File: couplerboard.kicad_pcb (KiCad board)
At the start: 2 copper layers, 48 x 33 mm, 15 parts, among them J1 X, J2 Y, J3 Z, J4 Conn_01x05, U1 LTV-817, U2 LTV-817, U3 LTV-817

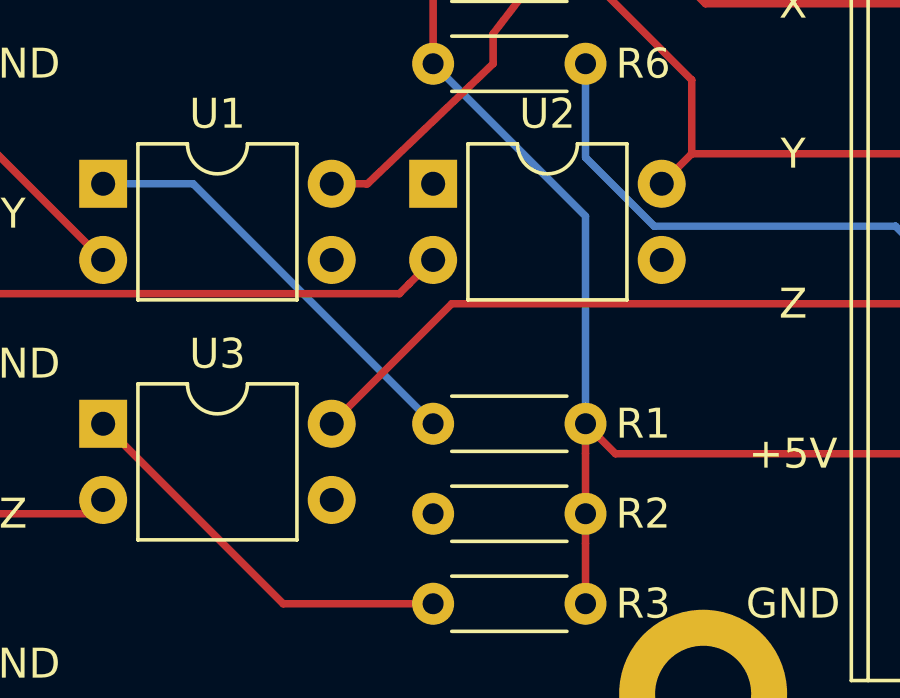
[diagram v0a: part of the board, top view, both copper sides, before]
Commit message: Fix missing route
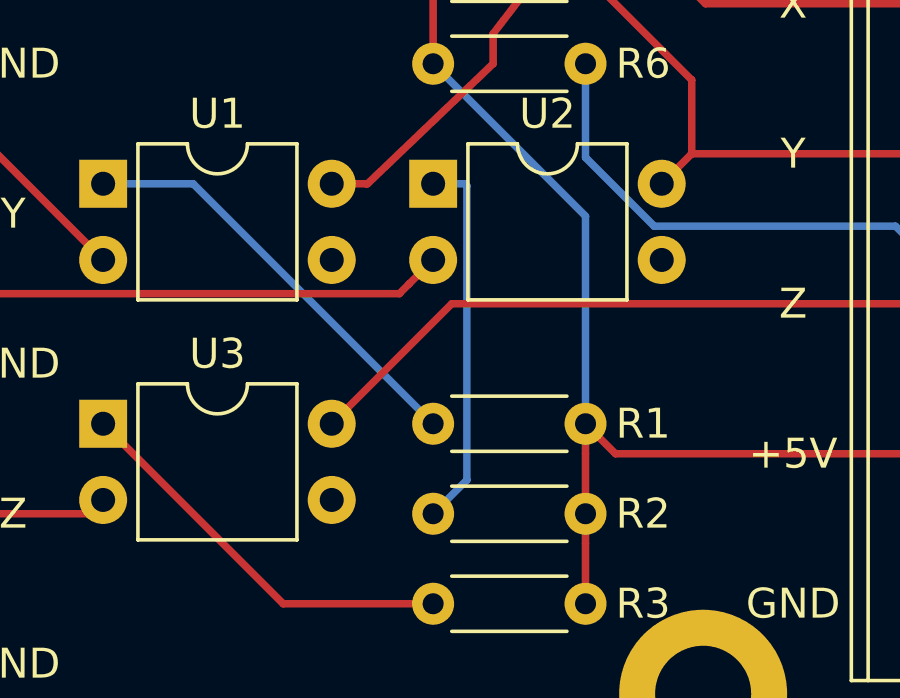
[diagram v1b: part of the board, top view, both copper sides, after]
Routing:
- net Net-(R2-Pad1): track 0.00 -> 12.5 mm
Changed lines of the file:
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@@
     (thickness 1.6)
     (drawings 15)
-    (tracks 42)
+    (tracks 46)
     (zones 0)
     (modules 15)
@@
   (segment (start 104 70) (end 112 78) (width 0.25) (layer B.Cu) (net 9))
   (segment (start 101 70) (end 104 70) (width 0.25) (layer B.Cu) (net 9))
+  (segment (start 113.05 70) (end 112 70) (width 0.25) (layer B.Cu) (net 10))
+  (segment (start 113.125001 70.075001) (end 113.05 70) (width 0.25) (layer B.Cu) (net 10))
+  (segment (start 113.125001 79.874999) (end 113.125001 70.075001) (width 0.25) (layer B.Cu) (net 10))
+  (segment (start 112 81) (end 113.125001 79.874999) (width 0.25) (layer B.Cu) (net 10))
   (segment (start 107 84) (end 101 78) (width 0.25) (layer F.Cu) (net 11))
   (segment (start 112 84) (end 107 84) (width 0.25) (layer F.Cu) (net 11))

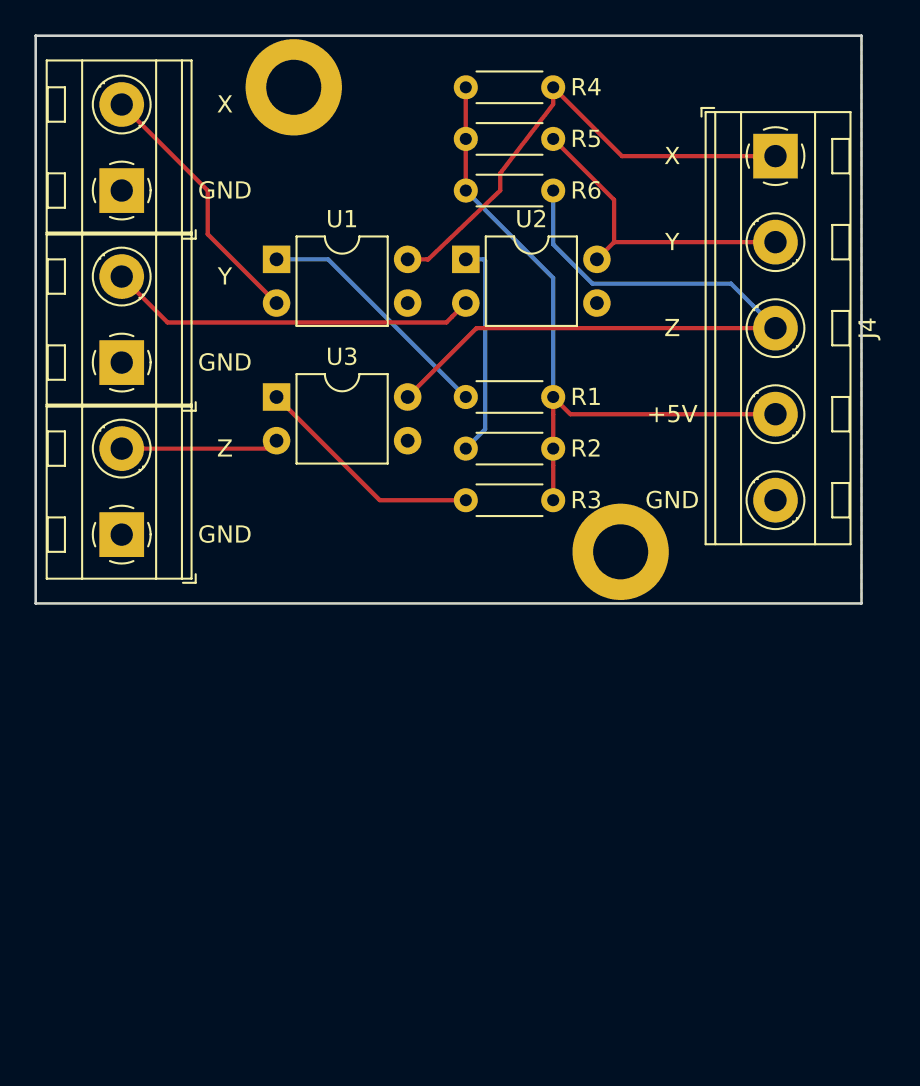
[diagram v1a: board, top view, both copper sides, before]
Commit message: Added mono jack for probe
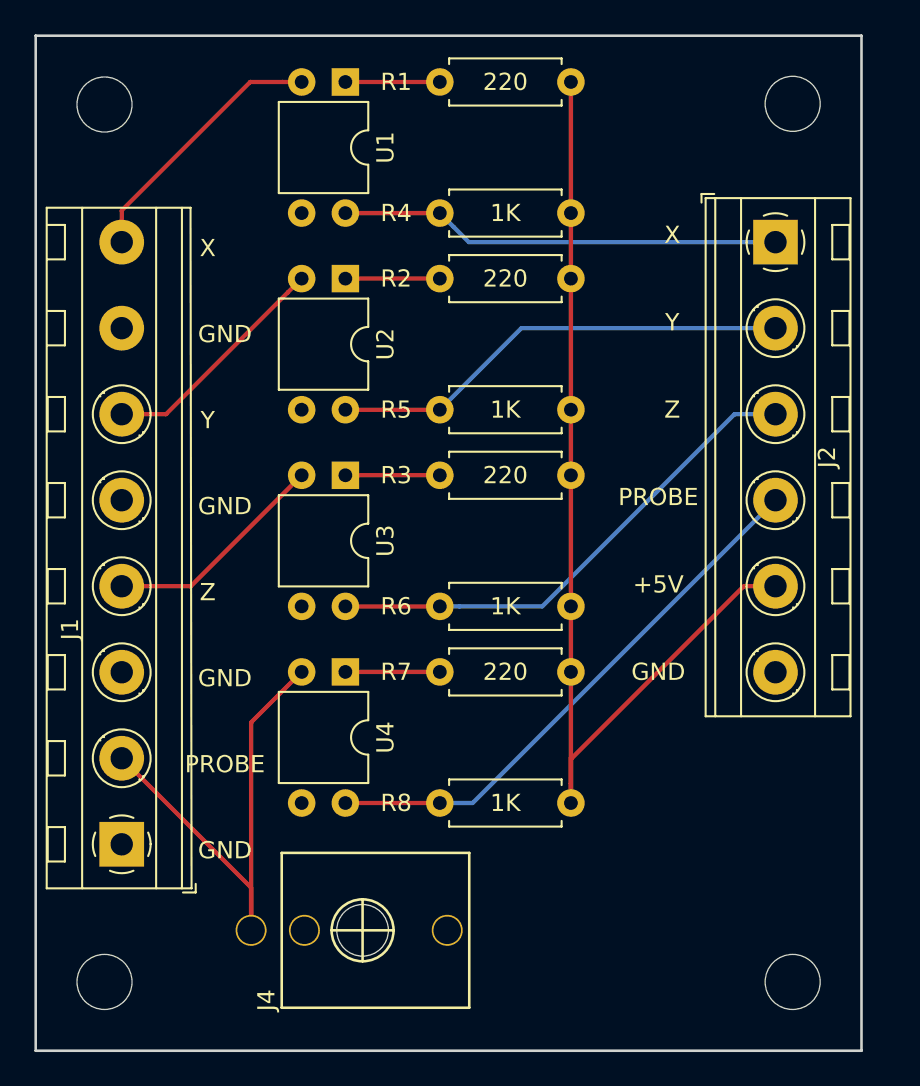
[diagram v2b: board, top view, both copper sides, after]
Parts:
- removed J3: Z, TerminalBlock_MetzConnect:TerminalBlock_MetzConnect_Type094_RT03502HBLU_1x02_P5.00mm_Horizontal
- added H3: MountingHole, MountingHole:MountingHole_3.2mm_M3_DIN965, F.Cu at (131.0, 112.0)
- added H4: MountingHole, MountingHole:MountingHole_3.2mm_M3_DIN965, F.Cu at (91.0, 61.0)
- added R7: 220, Resistor_THT:R_Axial_DIN0207_L6.3mm_D2.5mm_P7.62mm_Horizontal, F.Cu at (110.5, 94.0)
- added R8: 1K, Resistor_THT:R_Axial_DIN0207_L6.3mm_D2.5mm_P7.62mm_Horizontal, F.Cu at (118.1, 101.6)
- added U4: LTV-817, Package_DIP:DIP-4_W7.62mm, F.Cu at (105.0, 94.0)
- H1, H2: value MountingHole_Pad -> MountingHole; footprint MountingHole:MountingHole_3.2mm_M3_DIN965_Pad -> MountingHole:MountingHole_3.2mm_M3_DIN965
- J1: value X -> Conn_01x08; footprint TerminalBlock_MetzConnect:TerminalBlock_MetzConnect_Type094_RT03502HBLU_1x02_P5.00mm_Horizontal -> TerminalBlock_MetzConnect:TerminalBlock_MetzConnect_Type094_RT03506HBLU_1x08_P5.00mm_Horizontal
- J2: value Y -> Conn_01x06; footprint TerminalBlock_MetzConnect:TerminalBlock_MetzConnect_Type094_RT03502HBLU_1x02_P5.00mm_Horizontal -> TerminalBlock_MetzConnect:TerminalBlock_MetzConnect_Type094_RT03506HBLU_1x06_P5.00mm_Horizontal
- J4: value Conn_01x05 -> AudioJack2_SwitchT; footprint TerminalBlock_MetzConnect:TerminalBlock_MetzConnect_Type094_RT03505HBLU_1x05_P5.00mm_Horizontal -> Eurorack:ThonkIcon
- R1, R2, R3, R4, R5, R6: footprint Resistor_THT:R_Axial_DIN0204_L3.6mm_D1.6mm_P5.08mm_Horizontal -> Resistor_THT:R_Axial_DIN0207_L6.3mm_D2.5mm_P7.62mm_Horizontal
- moved H2 53.2 mm to (91.0, 112.0)
- moved J4 51.0 mm to (106.0, 109.0)
- moved J2 38.6 mm to (130.0, 69.0), turned to 270 degrees
- moved J1 38.0 mm to (92.0, 104.0)
- moved H1 27.9 mm to (131.0, 61.0)
- moved R6 24.9 mm to (118.1, 90.2), turned to 180 degrees
- moved R1 18.4 mm to (110.5, 59.7)
- moved R5 16.9 mm to (118.1, 78.7), turned to 180 degrees
- moved U1 11.1 mm to (105.0, 59.7), turned to 270 degrees
- moved R2 9.99 mm to (110.5, 71.1)
- moved R4 9.53 mm to (118.1, 67.3), turned to 180 degrees
- moved U2 7.09 mm to (105.0, 71.1), turned to 270 degrees
- moved U3 6.06 mm to (105.0, 82.5), turned to 270 degrees
- moved R3 2.09 mm to (110.5, 82.5)
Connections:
- H1 pad 1: GND -> (no net)
- H2 pad 1: GND -> (no net)
- J2 pad 1: GND -> /X
- J2 pad 2: Net-(J2-Pad2) -> /Y
- R4 pad 2: Net-(J4-Pad1) -> /X
- R5 pad 2: Net-(J4-Pad2) -> /Y
- R6 pad 2: Net-(J4-Pad3) -> /Z
- U1 pad 2: Net-(J1-Pad2) -> Net-(J1-Pad8)
- U1 pad 4: Net-(J4-Pad1) -> /X
- U2 pad 2: Net-(J2-Pad2) -> Net-(J1-Pad6)
- U2 pad 4: Net-(J4-Pad2) -> /Y
- U3 pad 2: Net-(J3-Pad2) -> Net-(J1-Pad4)
- U3 pad 4: Net-(J4-Pad3) -> /Z
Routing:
- net Net-(J4-Pad3): track 41.1 -> 0.00 mm
- net /P: track 0.00 -> 32.3 mm
- net /Z: track 0.00 -> 29.6 mm
- net Net-(J4-Pad1): track 28.6 -> 0.00 mm
- net /Y: track 0.00 -> 27.0 mm
- net /X: track 0.00 -> 25.7 mm
- net +5V: track 39.4 -> 63.2 mm
- net Net-(J2-Pad2): track 21.6 -> 0.00 mm
- net Net-(J4-Pad2): track 18.3 -> 0.00 mm
- net Net-(J1-Pad8): track 0.00 -> 15.4 mm
- net Net-(J1-Pad2): track 15.3 -> 29.4 mm
- net Net-(J1-Pad6): track 0.00 -> 13.7 mm
- net Net-(J1-Pad4): track 0.00 -> 13.1 mm
- net Net-(J3-Pad2): track 9.19 -> 0.00 mm
- net Net-(R1-Pad1): track 14.3 -> 5.49 mm
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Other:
- board size 48 x 33 mm -> 48 x 59 mm
- board text added: "Coupler Board v1.1"
- board text added: "PROBE"
- board text removed: "Limit Switch v1.0"

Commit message: WIP
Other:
- board text added: "Coupler Board"
- board text added: "inspired by https://github.com/gnea/grbl/wiki/Wiring-Limit-Switches - Github Repo: https://github.com/justjoheinz/couplerboard - v1.1"
- board text removed: "Coupler Board v1.1"
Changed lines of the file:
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@@
   (general
     (thickness 1.6)
-    (drawings 21)
+    (drawings 22)
     (tracks 45)
     (zones 0)
@@
     (34 B.Paste user)
     (35 F.Paste user)
-    (36 B.SilkS user)
+    (36 B.SilkS user hide)
     (37 F.SilkS user)
     (38 B.Mask user)
@@
     )
   )
+  (gr_text "inspired by\nhttps://github.com/gnea/grbl/wiki/Wiring-Limit-Switches\n-\nGithub Repo:\nhttps://github.com/justjoheinz/couplerboard\n-\nv1.1\n\n" (at 134.62 104.14) (layer B.SilkS)
+    (effects (font (size 1 1) (thickness 0.15)) (justify left mirror))
+  )
   (gr_text GND (at 98 104.35) (layer F.SilkS)
     (effects (font (size 1 1) (thickness 0.15)))
   )
-  (gr_text PROBE (at 98 99.35) (layer F.SilkS)
+  (gr_text PROBE (at 99.06 99.35) (layer F.SilkS)
     (effects (font (size 1 1) (thickness 0.15)))
   )
@@
     (effects (font (size 1 1) (thickness 0.15)))
   )
-  (gr_text "Coupler\nBoard\nv1.1" (at 133.35 82.55) (layer B.SilkS)
+  (gr_text "Coupler\nBoard\n" (at 134.62 82.55) (layer B.SilkS)
     (effects (font (size 8 8) (thickness 1.5)) (justify left mirror))
   )
@@
     (effects (font (size 1 1) (thickness 0.15)))
   )
-  (gr_text Endstops (at 91.44 107.95) (layer B.SilkS)
+  (gr_text Endstops (at 91.44 64.77) (layer B.SilkS)
     (effects (font (size 1 1) (thickness 0.15)) (justify mirror))
   )
-  (gr_text Arduino (at 130.81 107.95) (layer B.SilkS)
+  (gr_text Arduino (at 130.81 64.77) (layer B.SilkS)
     (effects (font (size 1 1) (thickness 0.15)) (justify mirror))
   )

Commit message: Reannotate
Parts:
- renumbered J4 to J1, J1 to J2, J2 to J3, R7 to R4, R4 to R5, R5 to R6, R6 to R7
